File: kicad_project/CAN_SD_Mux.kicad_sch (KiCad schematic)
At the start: 5 parts, among them U13 ADG733BRU

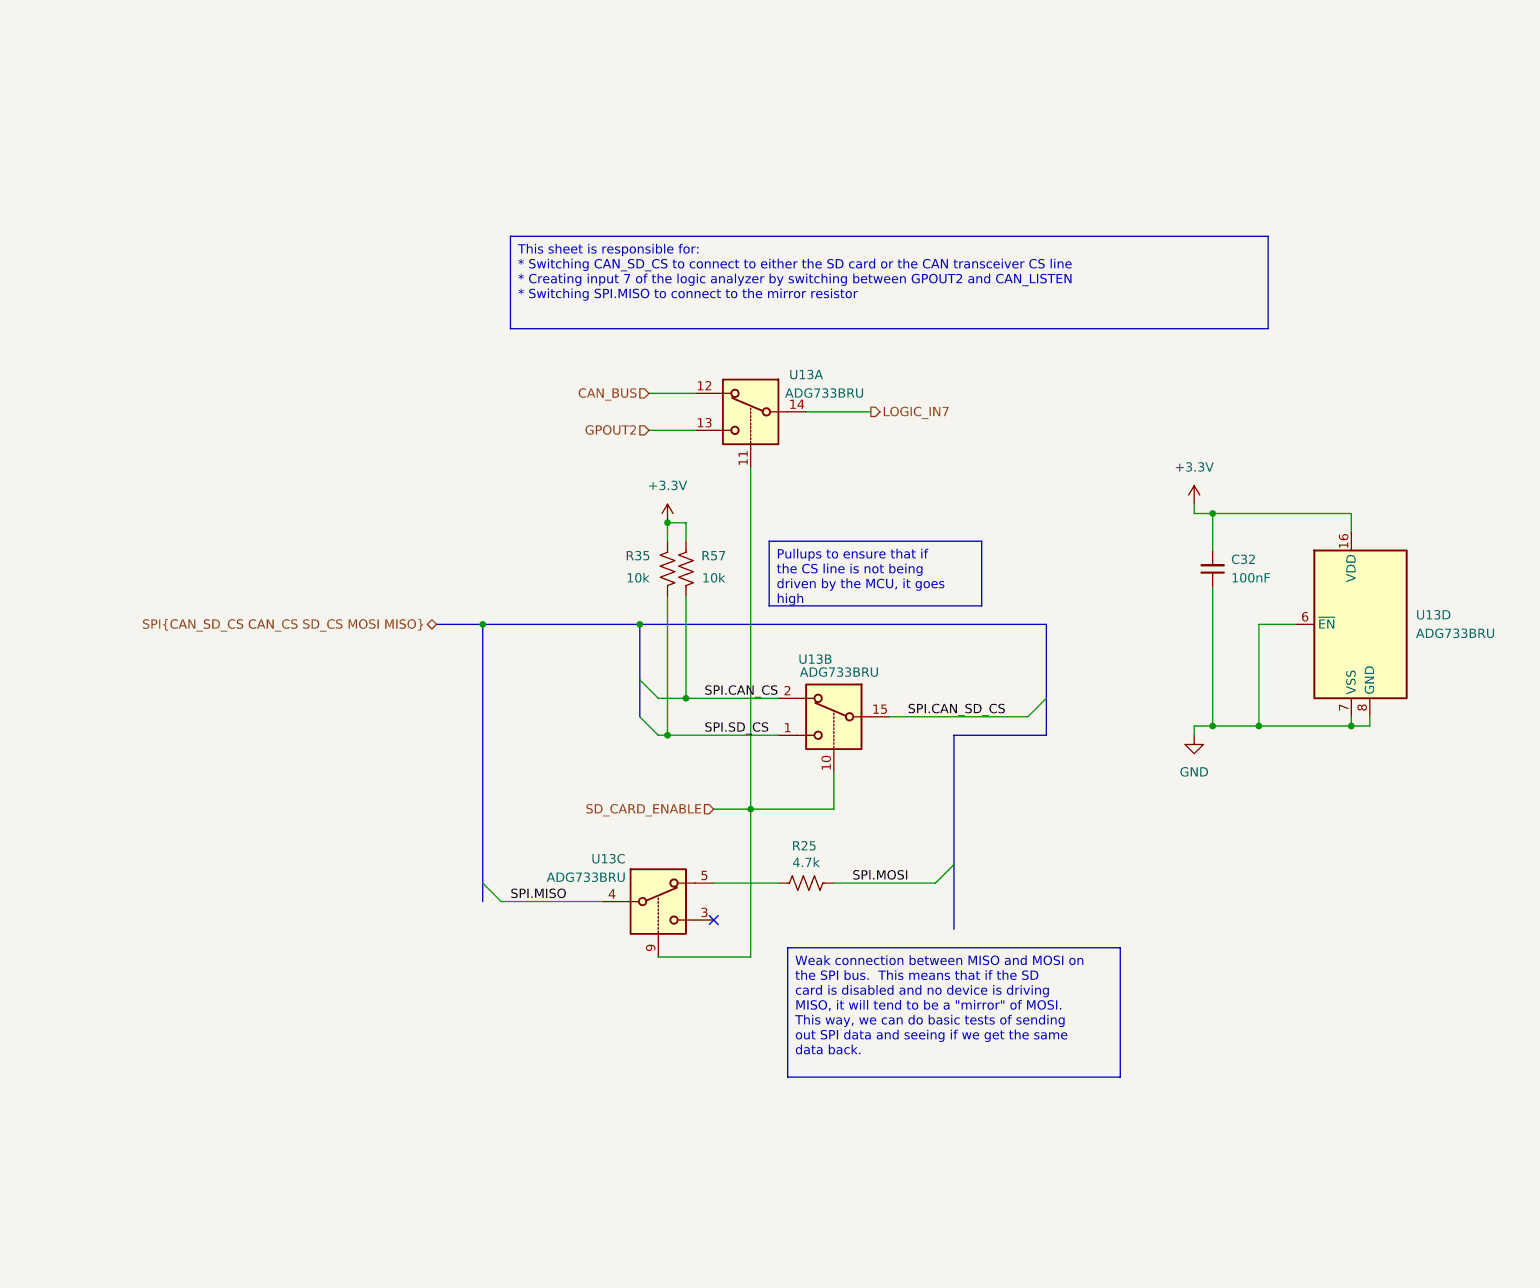
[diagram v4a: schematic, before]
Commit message: Switch out multiplexer, start switch FX2LP out for RP2040
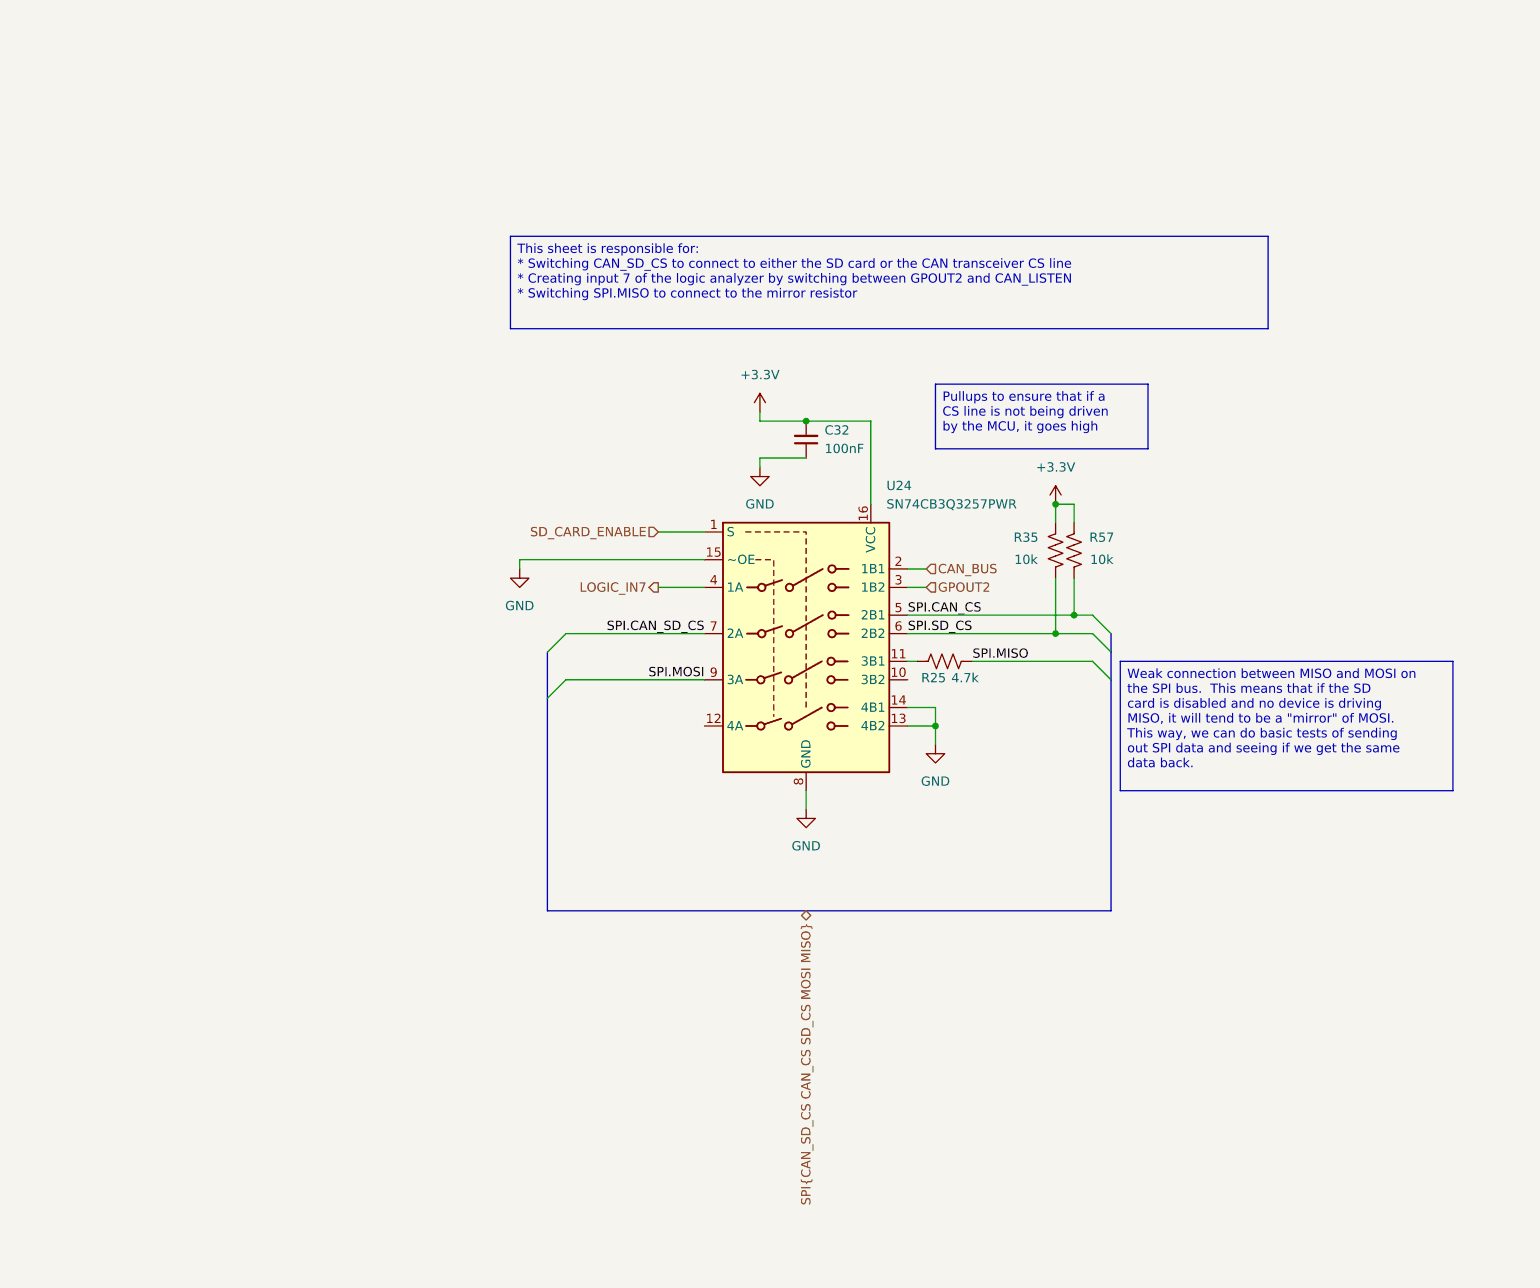
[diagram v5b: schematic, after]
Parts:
- removed U13: ADG733BRU, Package_SO:TSSOP-16_4.4x5mm_P0.65mm, symbol Analog_Switch:ADG733BRU
- added U24: SN74CB3Q3257PWR, Package_SO:TSSOP-16_4.4x5mm_P0.65mm, symbol project libraries:SN74CB3Q3257PWR
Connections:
- net +3.3V: now also U24.16 (VCC)
- net CAN_BUS: now also U24.2 (1B1)
- net GND: now also U24.13 (4B2), U24.14 (4B1), U24.15 (~OE), U24.8 (GND)
- net GPOUT2: now also U24.3 (1B2)
- net LOGIC_IN7: now also U24.4 (1A)
- net SD_CARD_ENABLE: now also U24.1 (S)
- net SPI.CAN_CS: now also U24.5 (2B1)
- net SPI.CAN_SD_CS: now also U24.7 (2A)
- net SPI.MISO: now also R25.2
- net SPI.MOSI: now also U24.9 (3A); no longer R25.2
- net SPI.SD_CS: now also U24.6 (2B2)
- net at R25.1: now also U24.11 (3B1)
- no-connect marks 1 -> 0
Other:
- moved on the sheet: C32, R25, R35, R57

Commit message: Start on Rev 4, switch to RPi Pico
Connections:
- no-connect marks 0 -> 2
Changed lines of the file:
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@@
 		(color 0 0 0 0)
+	)
+	(no_connect
+		(at 138.43 110.49)
+	)
+	(no_connect
+		(at 110.49 116.84)
 	)
 	(bus_entry
